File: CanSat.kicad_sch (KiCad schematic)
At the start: 39 parts, among them J1 USB_C_Receptacle, M1 SG-90, SW1 SW_MEC_5E, SW2 SW_MEC_5E, U1 MPU-6050, U6 LM1085-5.0, U7 LM1085-3.3, U8 BMP280

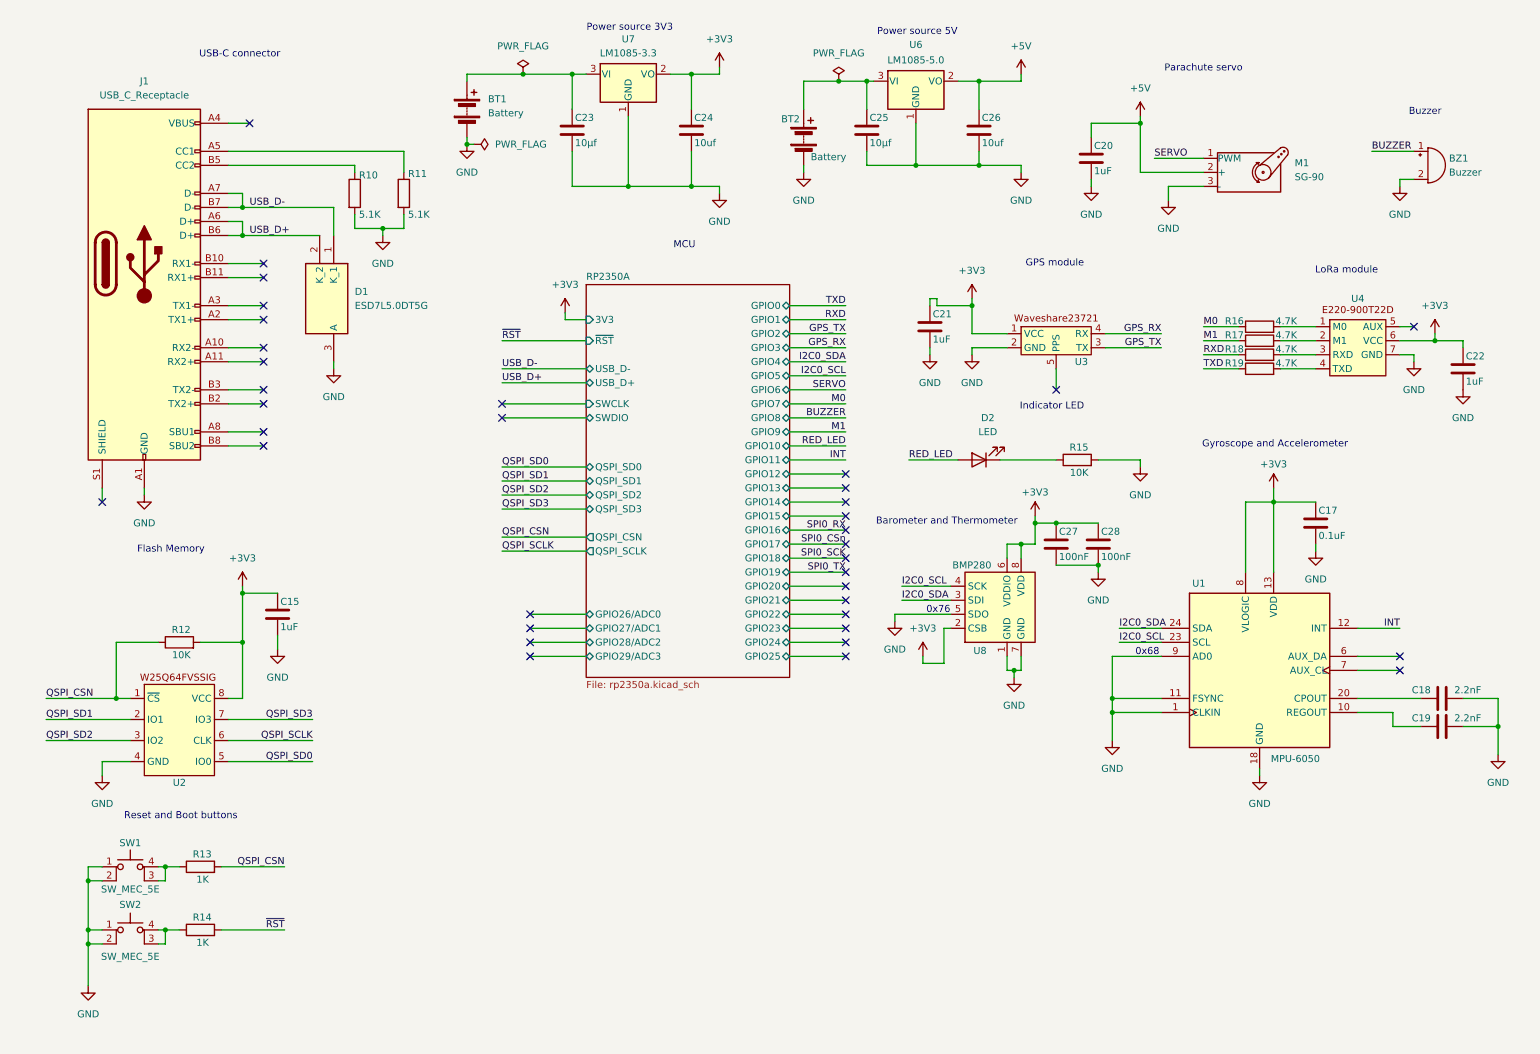
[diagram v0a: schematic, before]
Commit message: Add new flash memory and PSRAM
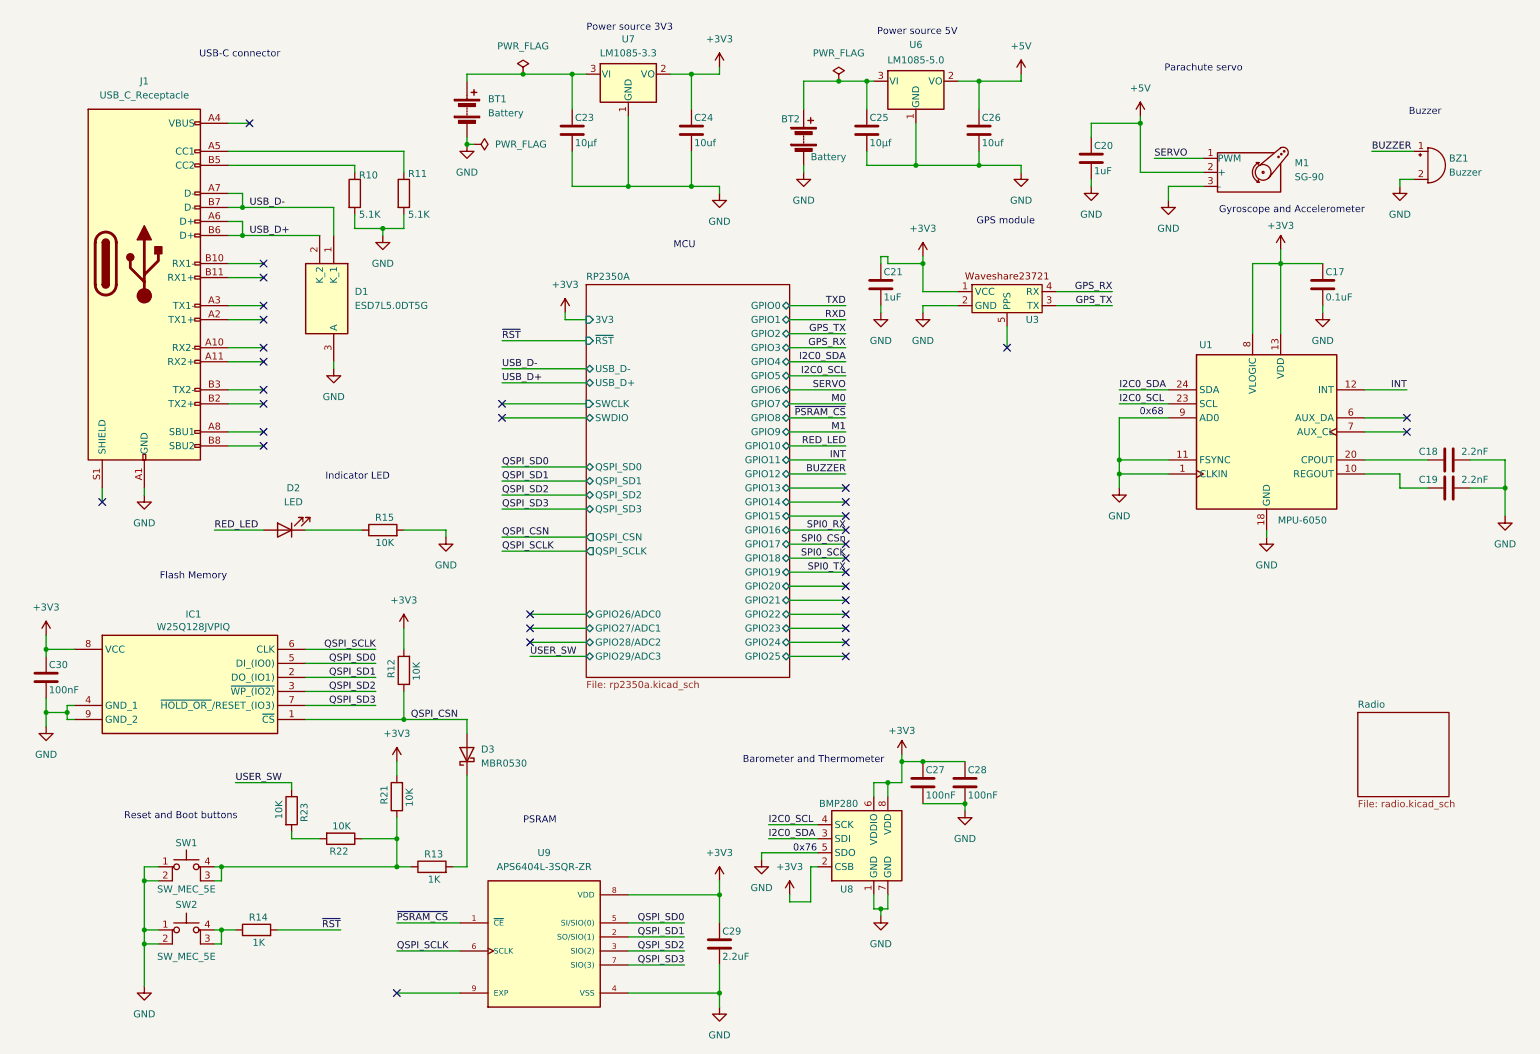
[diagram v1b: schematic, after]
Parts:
- removed C15, C22: 1uF, symbol Device:C
- removed R16, R17, R18, R19: 4.7K, symbol Device:R
- removed U2: ~, memory:W25Q64FVSSIG, symbol memory:W25Q64FVSSIG
- removed U4: ~, symbol LoRa:E220-900T22D
- added C29: 2.2uF, symbol Device:C
- added C30: 100nF, symbol Device:C
- added D3: MBR0530, Diode_SMD:D_SOD-123, symbol Diode:MBR0530
- added IC1: W25Q128JVPIQ, SON127P600X500X80-9N-D, symbol SamacSys_Parts:W25Q128JVPIQ
- added R21, R22, R23: 10K, Resistor_THT:R_Axial_DIN0207_L6.3mm_D2.5mm_P7.62mm_Horizontal, symbol Device:R
- added U9: APS6404L-3SQR-ZR, APS6404L-3SQR-ZR:PSON50P200X300X50-9N, symbol APS6404L-3SQR-ZR:APS6404L-3SQR-ZR
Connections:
- net +3V3: now also C29.1, C30.1, IC1.8 (VCC), R21.2, U9.8 (VDD)
- net GND: now also C29.2, C30.2, IC1.4 (GND_1), IC1.9 (GND_2), U9.4 (VSS)
- net QSPI_CSN: now also D3.2 (A), IC1.1 (~{CS}); no longer R13.2
- net QSPI_SCLK: now also IC1.6 (CLK), U9.6 (SCLK)
- net QSPI_SD0: now also IC1.5 (DI_(IO0)), U9.5 (SI/SIO(0))
- net QSPI_SD1: now also IC1.2 (DO_(IO1)), U9.2 (SO/SIO(1))
- net QSPI_SD2: now also IC1.3 (~{WP_(IO2)}), U9.3 (SIO(2))
- net QSPI_SD3: now also IC1.7 (~{HOLD_OR_}/RESET_(IO3)), U9.7 (SIO(3))
- net at R13.1, SW1.3 (K), SW1.4 (A): now also R21.1, R22.1
- new net: D3.1 (K), R13.2
- new net: R22.2, R23.2
- new net USER_SW: R23.1
- new net ~{PSRAM_CS}: U9.1 (~{CE})
- no-connect marks 36 -> 34
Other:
- added sheet Radio (radio.kicad_sch)
- note added: "PSRAM"
- note removed: "LoRa module"
- moved on the sheet: C17, C18, C19, C21, C27, C28, D2, R13, R14, R15, SW1, SW2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

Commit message: Add new LoRa module
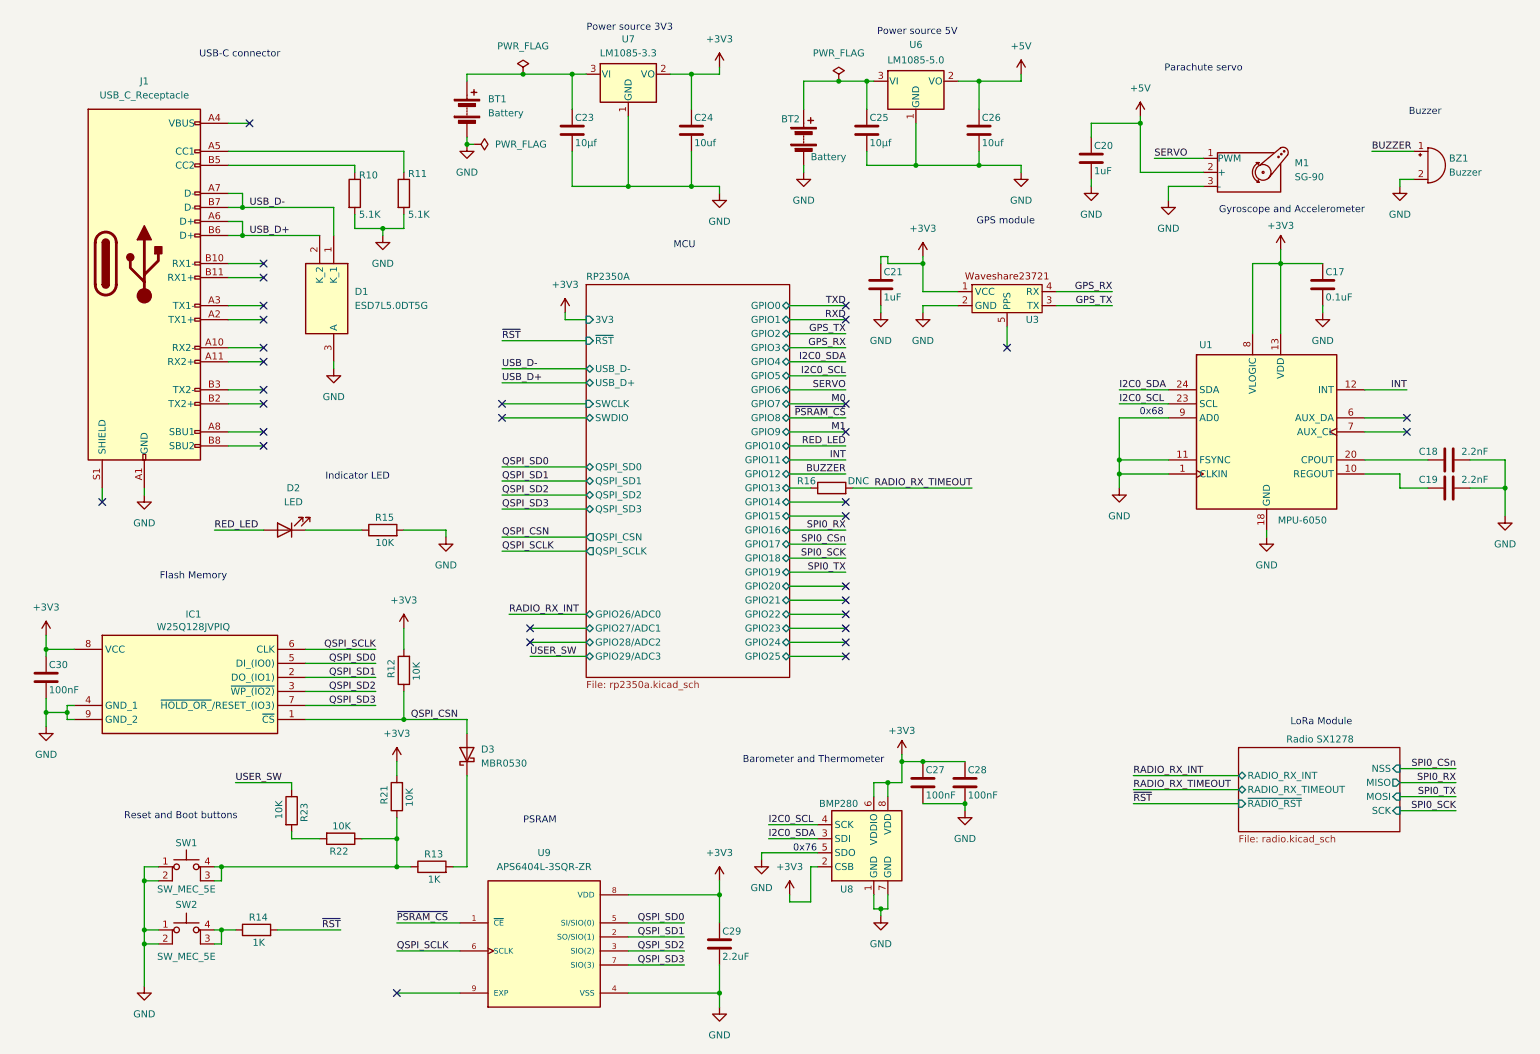
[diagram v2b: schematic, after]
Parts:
- added R16: DNC, symbol Device:R
- IC1: footprint SON127P600X500X80-9N-D -> SamacSys_Parts:SON127P600X500X80-9N-D
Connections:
- net RP2350A/GPIO13: now also R16.1
- new net RADIO_RX_TIMEOUT: R16.2
- no-connect marks 34 -> 32
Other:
- sheet Radio renamed Radio SX1278
- sheet Radio SX1278 ports: added MISO, MOSI, NSS, RADIO_RX_INT, RADIO_RX_TIMEOUT, SCK, ~{RADIO_RST}; removed none
- note added: "LoRa Module"

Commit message: Assigned footprints and drew pcb outline
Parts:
- BT1, BT2: footprint (none) -> Connector_PinHeader_1.00mm:PinHeader_1x02_P1.00mm_Vertical
- BZ1: footprint (none) -> Buzzer_Beeper:PUIAudio_SMT_0825_S_4_R
- C17, C18, C19, C20, C21, C23, C24, C25, C26, C27, C28, C29, C30: footprint (none) -> Capacitor_Tantalum_SMD:CP_EIA-2012-15_AVX-P
- D2: footprint (none) -> LED_SMD:LED_0402_1005Metric
- J1: footprint (none) -> Connector_USB:USB_C_Receptacle_Amphenol_124019772112A
- R10, R11, R12, R13, R14, R15, R21, R22, R23: footprint Resistor_THT:R_Axial_DIN0207_L6.3mm_D2.5mm_P7.62mm_Horizontal -> Resistor_SMD:R_0805_2012Metric
- R16: footprint (none) -> Resistor_SMD:R_0805_2012Metric
- SW1, SW2: footprint (none) -> Button_Switch_SMD:Panasonic_EVQPUL_EVQPUC
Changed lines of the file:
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@@
 			)
 		)
-		(property "Footprint" ""
+		(property "Footprint" "Capacitor_Tantalum_SMD:CP_EIA-2012-15_AVX-P"
 			(at 115.2652 38.1 0)
 			(effects
@@
 			)
 		)
-		(property "Footprint" "Resistor_THT:R_Axial_DIN0207_L6.3mm_D2.5mm_P7.62mm_Horizontal"
+		(property "Footprint" "Resistor_SMD:R_0805_2012Metric"
 			(at 88.9 169.418 90)
 			(effects
@@
 			)
 		)
-		(property "Footprint" "Resistor_THT:R_Axial_DIN0207_L6.3mm_D2.5mm_P7.62mm_Horizontal"
+		(property "Footprint" "Resistor_SMD:R_0805_2012Metric"
 			(at 80.01 108.458 90)
 			(effects
@@
 			)
 		)
-		(property "Footprint" "Resistor_THT:R_Axial_DIN0207_L6.3mm_D2.5mm_P7.62mm_Horizontal"
+		(property "Footprint" "Resistor_SMD:R_0805_2012Metric"
 			(at 61.722 157.48 90)
 			(effects
@@
 			)
 		)
-		(property "Footprint" ""
+		(property "Footprint" "Capacitor_Tantalum_SMD:CP_EIA-2012-15_AVX-P"
 			(at 171.1452 66.04 0)
 			(effects
@@
 			)
 		)
-		(property "Footprint" "Resistor_THT:R_Axial_DIN0207_L6.3mm_D2.5mm_P7.62mm_Horizontal"
+		(property "Footprint" "Resistor_SMD:R_0805_2012Metric"
 			(at 57.15 180.848 90)
 			(effects
@@
 			)
 		)
-		(property "Footprint" ""
+		(property "Footprint" "Capacitor_Tantalum_SMD:CP_EIA-2012-15_AVX-P"
 			(at 178.7652 156.21 0)
 			(effects
@@
 			)
 		)
-		(property "Footprint" ""
+		(property "Footprint" "Connector_PinHeader_1.00mm:PinHeader_1x02_P1.00mm_Vertical"
 			(at 95.25 28.956 90)
 			(effects
@@
 			)
 		)
-		(property "Footprint" ""
+		(property "Footprint" "Buzzer_Beeper:PUIAudio_SMT_0825_S_4_R"
 			(at 268.605 38.1 90)
 			(effects
@@
 			)
 		)
-		(property "Footprint" ""
+		(property "Footprint" "Button_Switch_SMD:Panasonic_EVQPUL_EVQPUC"
 			(at 44.45 162.56 0)
 			(effects
@@
 			)
 		)
-		(property "Footprint" "Resistor_THT:R_Axial_DIN0207_L6.3mm_D2.5mm_P7.62mm_Horizontal"
+		(property "Footprint" "Resistor_SMD:R_0805_2012Metric"
 			(at 85.598 132.08 90)
 			(effects
@@
 			)
 		)
-		(property "Footprint" ""
+		(property "Footprint" "Connector_USB:USB_C_Receptacle_Amphenol_124019772112A"
 			(at 40.64 58.42 0)
 			(effects
@@
 			)
 		)
-		(property "Footprint" ""
+		(property "Footprint" "LED_SMD:LED_0402_1005Metric"
 			(at 62.23 106.68 0)
 			(effects
@@
 			)
 		)
-		(property "Footprint" ""
+		(property "Footprint" "Connector_PinHeader_1.00mm:PinHeader_1x02_P1.00mm_Vertical"
 			(at 156.21 34.036 90)
 			(effects
@@
 			)
 		)
-		(property "Footprint" "Resistor_THT:R_Axial_DIN0207_L6.3mm_D2.5mm_P7.62mm_Horizontal"
+		(property "Footprint" "Resistor_SMD:R_0805_2012Metric"
 			(at 72.39 160.782 90)
 			(effects
@@
 			)
 		)
-		(property "Footprint" ""
+		(property "Footprint" "Capacitor_Tantalum_SMD:CP_EIA-2012-15_AVX-P"
 			(at 141.9352 185.42 0)
 			(effects
@@
 			)
 		)
-		(property "Footprint" ""
+		(property "Footprint" "Resistor_SMD:R_0805_2012Metric"
 			(at 161.29 100.838 90)
 			(effects
@@
 			)
 		)
-		(property "Footprint" "Resistor_THT:R_Axial_DIN0207_L6.3mm_D2.5mm_P7.62mm_Horizontal"
+		(property "Footprint" "Resistor_SMD:R_0805_2012Metric"
 			(at 73.152 45.72 90)
 			(effects
@@
 			)
 		)
-		(property "Footprint" ""
+		(property "Footprint" "Capacitor_Tantalum_SMD:CP_EIA-2012-15_AVX-P"
 			(at 276.86 93.0148 0)
 			(effects
@@
 			)
 		)
-		(property "Footprint" ""
+		(property "Footprint" "Capacitor_Tantalum_SMD:CP_EIA-2012-15_AVX-P"
 			(at 186.3852 156.21 0)
 			(effects
@@
 			)
 		)
-		(property "Footprint" ""
+		(property "Footprint" "Capacitor_Tantalum_SMD:CP_EIA-2012-15_AVX-P"
 			(at 168.6052 38.1 0)
 			(effects
@@
 			)
 		)
-		(property "Footprint" "Resistor_THT:R_Axial_DIN0207_L6.3mm_D2.5mm_P7.62mm_Horizontal"
+		(property "Footprint" "Resistor_SMD:R_0805_2012Metric"
 			(at 84.328 154.94 90)
 			(effects
@@
 			)
 		)
-		(property "Footprint" ""
+		(property "Footprint" "Capacitor_Tantalum_SMD:CP_EIA-2012-15_AVX-P"
 			(at 20.0152 137.16 0)
 			(effects
@@
 			)
 		)
-		(property "Footprint" ""
+		(property "Footprint" "Capacitor_Tantalum_SMD:CP_EIA-2012-15_AVX-P"
 			(at 251.1552 66.04 0)
 			(effects
@@
 			)
 		)
-		(property "Footprint" ""
+		(property "Footprint" "Button_Switch_SMD:Panasonic_EVQPUL_EVQPUC"
 			(at 44.45 173.99 0)
 			(effects
@@
 			)
 		)
-		(property "Footprint" ""
+		(property "Footprint" "Capacitor_Tantalum_SMD:CP_EIA-2012-15_AVX-P"
 			(at 209.2452 43.18 0)
 			(effects
@@
 			)
 		)
-		(property "Footprint" ""
+		(property "Footprint" "Capacitor_Tantalum_SMD:CP_EIA-2012-15_AVX-P"
 			(at 188.9252 38.1 0)
 			(effects
@@
 			)
 		)
-		(property "Footprint" ""
+		(property "Footprint" "Capacitor_Tantalum_SMD:CP_EIA-2012-15_AVX-P"
 			(at 276.86 98.0948 0)
 			(effects
@@
 			)
 		)
-		(property "Footprint" "Resistor_THT:R_Axial_DIN0207_L6.3mm_D2.5mm_P7.62mm_Horizontal"
+		(property "Footprint" "Resistor_SMD:R_0805_2012Metric"
 			(at 82.042 45.72 90)
 			(effects
@@
 			)
 		)
-		(property "Footprint" ""
+		(property "Footprint" "Capacitor_Tantalum_SMD:CP_EIA-2012-15_AVX-P"
 			(at 136.8552 38.1 0)
 			(effects
